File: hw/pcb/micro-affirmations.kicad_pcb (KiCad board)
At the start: 2 copper layers, 70 x 40 mm, 165 parts, among them J1 USBC, J2 DEBUG, Q1 NCH, Q10 NCH, Q2 NCH, Q3 NCH, Q4 NCH, Q5 NCH, Q6 NCH, Q7 NCH, Q8 NCH, Q9 NCH, SW1 RST, U1 STM32C031C6Tx, U2 TPS61094

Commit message: chore: exported hardware revision d files
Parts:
- moved TP7 9.78 mm to (181.4, 106.9)
- moved TP6 1.20 mm to (181.8, 100.8)
- moved G*** 0.80 mm to (159.6, 106.0)
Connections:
- TP7 pad 1: Net-(U1-PA0) -> Net-(U1-PB7)
- U1 pad 11: Net-(U1-PA0) -> CAP_VOLT
- U1 pad 46: CAP_VOLT -> Net-(U1-PB7)
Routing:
- net CAP_VOLT: track 41.0 -> 49.9 mm
- net GND: track 62.1 -> 64.6 mm
- net /CHARGE_SENSE: track 28.3 -> 25.9 mm
- net Net-(U1-PA0): track 2.30 -> 0.00 mm, vias 1 -> 0
- net +3V3: track 28.4 -> 26.3 mm, vias 1 -> 0
- net Net-(U1-PB7): track 0.00 -> 1.71 mm, vias 0 -> 1
- net Net-(U1-PC13): track 3.55 -> 2.61 mm
- net /DEBUG_SWDIO: track 23.3 -> 22.5 mm
- net /NRST: track 38.9 -> 38.1 mm
- net /MATRIX_A7: track 15.2 -> 15.9 mm

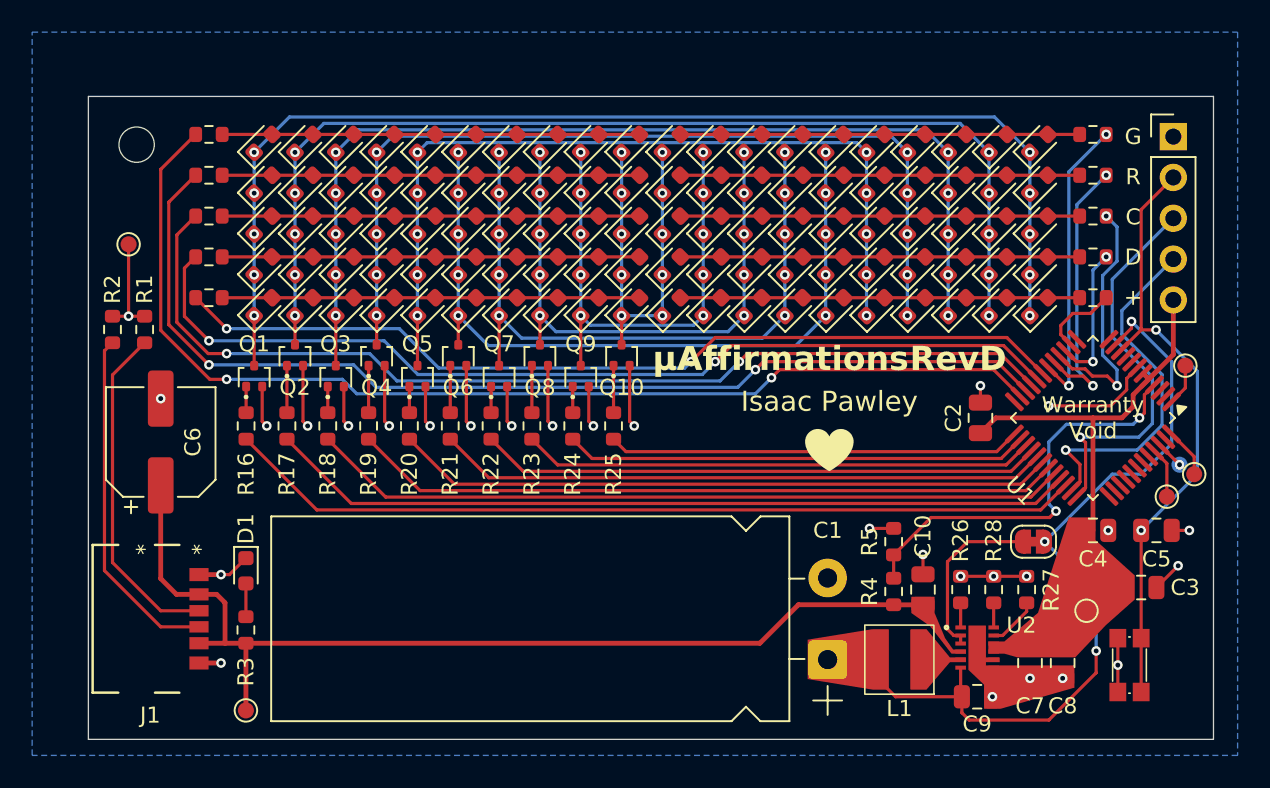
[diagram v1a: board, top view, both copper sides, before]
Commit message: fix: updated schematics to pcb revision d
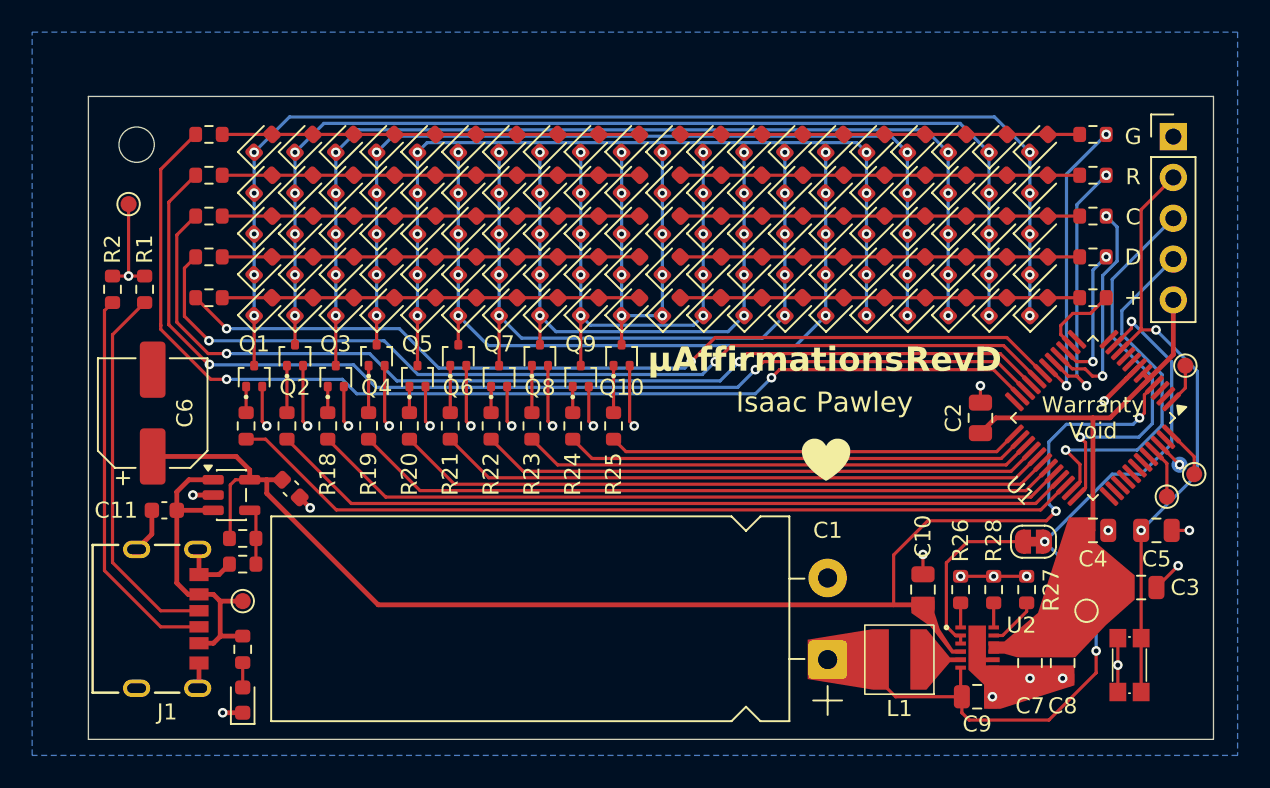
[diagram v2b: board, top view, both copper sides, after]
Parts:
- removed R4: 5.1k, Resistor_SMD:R_0603_1608Metric
- removed R5: 10k, Resistor_SMD:R_0603_1608Metric
- added C11: 1u, Capacitor_SMD:C_0603_1608Metric, F.Cu at (118.2, 109.8)
- added C12: 1u, Capacitor_SMD:C_0603_1608Metric, F.Cu at (126.1, 108.4)
- added R29: 33k, Resistor_SMD:R_0603_1608Metric, F.Cu at (123.1, 111.5)
- added R30: 10k, Resistor_SMD:R_0603_1608Metric, F.Cu at (123.1, 113.1)
- added U3: LDK130, Package_TO_SOT_SMD:SOT-23-5, F.Cu at (122.4, 108.8)
- J1: value USBC -> USB-C
- moved D1 8.05 mm to (123.1, 121.6), turned to 90 degrees
- moved TP2 6.80 mm to (123.1, 115.4)
- moved R1 2.50 mm to (117.0, 96.0)
- moved R2 2.50 mm to (115.0, 96.0)
- moved TP8 2.50 mm to (116.0, 90.7)
- moved C6 1.87 mm to (117.5, 103.7)
- moved R3 1.22 mm to (123.1, 118.4), turned to -90 degrees
- moved G*** 0.63 mm to (159.4, 106.6)
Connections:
- C10 pad 1: +5V -> /CHARGE_SENSE
- C6 pad 1: +5V -> /CHARGE_SENSE
- U2 pad 4: +5V -> /CHARGE_SENSE
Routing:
- net /CHARGE_SENSE: track 25.9 -> 85.8 mm
- net +5V: track 63.2 -> 20.2 mm
- net Net-(U3-ADJ): track 0.00 -> 3.74 mm
- net Net-(J1-CC2): track 21.7 -> 24.2 mm
- net Net-(J1-CC1): track 21.1 -> 23.6 mm
- net /MATRIX_A7: track 15.9 -> 13.8 mm
- net GND: track 64.6 -> 65.9 mm, vias 28 -> 27
- net /MATRIX_A6: track 17.3 -> 16.7 mm
- net Net-(D1-A): track 2.07 -> 1.55 mm

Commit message: fix: added or-ing diode to board
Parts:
- removed JP1: SolderJumper_2_Bridged, Jumper:SolderJumper-2_P1.3mm_Bridged_RoundedPad1.0x1.5mm
- added D2: ~, Package_TO_SOT_SMD:SOT-23, F.Cu at (165.1, 112.6)
- moved C10 3.25 mm to (162.2, 115.0)
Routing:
- net CAP_VOLT: track 49.9 -> 56.8 mm
- net /CHARGE_SENSE: track 85.8 -> 91.3 mm
- net GND: track 65.9 -> 71.1 mm, vias 27 -> 30
- net Net-(D2-K): track 10.9 -> 5.76 mm

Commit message: chore: finalised pcb for rev d export
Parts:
- removed G***: LOGO, LOGO
- R28: value 13.0k -> 13.0k*
- R29: value 33k -> 33k*
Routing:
- net /CHARGE_SENSE: track 91.3 -> 90.6 mm
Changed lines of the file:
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@@
 		(filling no)
 		(pcbplotparams
-			(layerselection 0x00000000_00000000_55555555_5755f5ff)
+			(layerselection 0x00000000_00000000_55555555_555555d0)
 			(plot_on_all_layers_selection 0x00000000_00000000_00000000_00000000)
 			(disableapertmacros no)
@@
 			(drillshape 0)
 			(scaleselection 1)
-			(outputdirectory "gerbers/RevD/")
+			(outputdirectory "gerbers/RevD-not/")
 		)
 	)
@@
 			)
 		)
-		(property "Value" "33k"
+		(property "Value" "33k*"
 			(at 0 1.43 0)
 			(layer "F.Fab")
@@
 		)
 	)
-	(footprint "LOGO"
-		(layer "F.Cu")
-		(at 159.397825 106.6)
-		(property "Reference" "G***"
-			(at 0 0 0)
-			(layer "F.SilkS")
-			(hide yes)
-			(effects
-				(font
-					(size 1.5 1.5)
-					(thickness 0.3)
-				)
-			)
-		)
-		(property "Value" "LOGO"
-			(at 0.75 0 0)
-			(layer "F.SilkS")
-			(hide yes)
-			(effects
-				(font
-					(size 1.5 1.5)
-					(thickness 0.3)
-				)
-			)
-		)
-		(property "Datasheet" ""
-			(at 0 0 0)
-			(layer "F.Fab")
-			(hide yes)
-			(effects
-				(font
-					(size 1.27 1.27)
-				)
-			)
-		)
-		(property "Description" ""
-			(at 0 0 0)
-			(layer "F.Fab")
-			(hide yes)
-			(effects
-				(font
-					(size 1.27 1.27)
-				)
-			)
-		)
-		(attr board_only exclude_from_pos_files exclude_from_bom)
-		(duplicate_pad_numbers_are_jumpers no)
-		(fp_poly
-			(pts
-				(xy 0.771563 -1.309687) (xy 0.835853 -1.302839) (xy 0.844934 -1.30143) (xy 0.909498 -1.288299) (xy 0.972175 -1.270069)
-				(xy 1.032758 -1.246845) (xy 1.091044 -1.218734) (xy 1.146829 -1.185839) (xy 1.199906 -1.148266)
-				(xy 1.250073 -1.106119) (xy 1.278387 -1.078985) (xy 1.318838 -1.035563) (xy 1.354602 -0.991192)
-				(xy 1.386458 -0.944789) (xy 1.415188 -0.895275) (xy 1.425651 -0.875014) (xy 1.451398 -0.818801)
-				(xy 1.472115 -0.7629) (xy 1.48801 -0.706469) (xy 1.499293 -0.648667) (xy 1.506173 -0.588651) (xy 1.508576 -0.541415)
-				(xy 1.507749 -0.467586) (xy 1.501492 -0.393197) (xy 1.489811 -0.318266) (xy 1.472714 -0.242808)
-				(xy 1.450209 -0.166842) (xy 1.422303 -0.090383) (xy 1.389004 -0.013449) (xy 1.350318 0.063943) (xy 1.306254 0.141776)
-				(xy 1.256819 0.220035) (xy 1.20202 0.298701) (xy 1.141865 0.377758) (xy 1.076362 0.457189) (xy 1.054578 0.482335)
-				(xy 0.98928 0.554219) (xy 0.918979 0.626625) (xy 0.844076 0.699219) (xy 0.764967 0.771666) (xy 0.682053 0.843632)
-				(xy 0.595733 0.914782) (xy 0.506404 0.984782) (xy 0.414467 1.053298) (xy 0.320321 1.119994) (xy 0.224363 1.184537)
-				(xy 0.191787 1.20568) (xy 0.173831 1.21713) (xy 0.154526 1.229268) (xy 0.134511 1.241708) (xy 0.114423 1.254065)
-				(xy 0.094901 1.265953) (xy 0.076583 1.276986) (xy 0.060106 1.286779) (xy 0.046107 1.294946) (xy 0.035227 1.301102)
-				(xy 0.028101 1.30486) (xy 0.026577 1.305552) (xy 0.008703 1.310339) (xy -0.009174 1.310364) (xy -0.016498 1.308867)
-				(xy -0.023885 1.30596) (xy -0.035356 1.300271) (xy -0.050462 1.292076) (xy -0.06875 1.281648) (xy -0.089768 1.26926)
-				(xy -0.113066 1.255186) (xy -0.138193 1.239699) (xy -0.164695 1.223072) (xy -0.192123 1.205581)
-				(xy -0.220024 1.187497) (xy -0.247948 1.169094) (xy -0.255631 1.163974) (xy -0.361281 1.091427)
-				(xy -0.46365 1.017192) (xy -0.562475 0.941493) (xy -0.657497 0.864556) (xy -0.748453 0.786609) (xy -0.835084 0.707877)
-				(xy -0.917127 0.628586) (xy -0.994322 0.548962) (xy -1.066408 0.469231) (xy -1.091317 0.440241)
-				(xy -1.156319 0.360387) (xy -1.215859 0.28074) (xy -1.269939 0.201295) (xy -1.318559 0.12205) (xy -1.361723 0.042999)
-				(xy -1.399433 -0.035861) (xy -1.43169 -0.114535) (xy -1.458497 -0.193026) (xy -1.479855 -0.27134)
-				(xy -1.495767 -0.34948) (xy -1.501471 -0.386921) (xy -1.504292 -0.412133) (xy -1.506477 -0.440744)
-				(xy -1.508004 -0.471455) (xy -1.508848 -0.50297) (xy -1.508987 -0.533992) (xy -1.508396 -0.563225)
-				(xy -1.507054 -0.589371) (xy -1.50544 -0.607041) (xy -1.498162 -0.658342) (xy -1.488425 -0.706263)
-				(xy -1.475799 -0.752259) (xy -1.459856 -0.79778) (xy -1.440167 -0.844279) (xy -1.427529 -0.870912)
-				(xy -1.401953 -0.91915) (xy -1.374172 -0.963814) (xy -1.343342 -1.006082) (xy -1.308617 -1.047134)
-				(xy -1.278366 -1.078985) (xy -1.230498 -1.123353) (xy -1.179602 -1.163279) (xy -1.125974 -1.198665)
-				(xy -1.069908 -1.229411) (xy -1.011696 -1.255422) (xy -0.951635 -1.276598) (xy -0.890016 -1.292843)
-				(xy -0.827136 -1.304057) (xy -0.763287 -1.310145) (xy -0.698764 -1.311007) (xy -0.633862 -1.306545)
-				(xy -0.605216 -1.302864) (xy -0.541709 -1.290799) (xy -0.479717 -1.27359) (xy -0.41953 -1.251421)
-				(xy -0.361439 -1.224479) (xy -0.305736 -1.192949) (xy -0.252712 -1.157018) (xy -0.202658 -1.11687)
-				(xy -0.155865 -1.072691) (xy -0.112625 -1.024667) (xy -0.073228 -0.972984) (xy -0.062003 -0.956494)
-				(xy -0.050706 -0.938917) (xy -0.039399 -0.920388) (xy -0.028708 -0.902008) (xy -0.01926 -0.884882)
-				(xy -0.01168 -0.87011) (xy -0.006763 -0.859221) (xy -0.00359 -0.852322) (xy -0.000892 -0.848192)
-				(xy -0.000068 -0.84767) (xy 0.002039 -0.849978) (xy 0.005261 -0.855918) (xy 0.007693 -0.861358)
-				(xy 0.015176 -0.877406) (xy 0.025488 -0.896692) (xy 0.038002 -0.918218) (xy 0.05209 -0.940984) (xy 0.067124 -0.963992)
-				(xy 0.082476 -0.986242) (xy 0.097519 -1.006738) (xy 0.105676 -1.017204) (xy 0.130823 -1.046493)
-				(xy 0.159878 -1.076634) (xy 0.191638 -1.106533) (xy 0.224902 -1.135095) (xy 0.258465 -1.161227)
-				(xy 0.282732 -1.178319) (xy 0.338023 -1.212108) (xy 0.39569 -1.241091) (xy 0.455374 -1.26519) (xy 0.51672 -1.284327)
-				(xy 0.579369 -1.298423) (xy 0.642964 -1.307401) (xy 0.707148 -1.311181)
-			)
-			(stroke
-				(width 0)
-				(type solid)
-			)
-			(fill yes)
-			(layer "F.SilkS")
-		)
-		(embedded_fonts no)
-	)
 	(footprint "Diode_SMD:D_0603_1608Metric"
 		(layer "F.Cu")
@@
 		(sheetname "/supercapacitor-charger/")
 		(sheetfile "supercapacitor-charger.kicad_sch")
+		(units
+			(unit
+				(name "A")
+				(pins "1" "2")
+			)
+		)
 		(attr smd)
 		(duplicate_pad_numbers_are_jumpers no)
@@
 			)
 		)
-		(property "Value" "13.0k"
+		(property "Value" "13.0k*"
 			(at 0 1.43 90)
 			(layer "F.Fab")
@@
 	)
 	(segment
-		(start 165.132182 116)
+		(start 164.15 116)
 		(end 162.2 116)
 		(width 0.3)
@@
 	)
 	(segment
-		(start 164.15 114.25)
-		(end 162.4 116)
-		(width 0.2)
-		(layer "F.Cu")
-		(net "/CHARGE_SENSE")
-	)
-	(segment
 		(start 122.69375 106.4)
 		(end 123.5375 107.24375)
@@
 	)
 	(segment
-		(start 179.2 103.7)
-		(end 179.2 102.567766)
+		(start 164.15 111.7)
+		(end 164.15 116)
 		(width 0.2)
 		(layer "F.Cu")
@@
 	)
 	(segment
-		(start 164.15 111.7)
-		(end 164.15 114.25)
+		(start 179.2 103.7)
+		(end 179.2 102.567766)
 		(width 0.2)
 		(layer "F.Cu")
@@
 	)
 	(segment
+		(start 165.132182 116)
+		(end 164.15 116)
+		(width 0.3)
+		(layer "F.Cu")
+		(net "/CHARGE_SENSE")
+	)
+	(segment
 		(start 122.325 111.45)
 		(end 122.325 108.175)
@@
 	)
 	(segment
+		(start 165.1 115.19)
+		(end 167.449622 117.539622)
+		(width 0.2)
+		(layer "F.Cu")
+		(net "Net-(D2-K)")
+	)
+	(segment
+		(start 167.767 118.039748)
+		(end 167.767 117.539622)
+		(width 0.2)
+		(layer "F.Cu")
+		(net "Net-(D2-K)")
+	)
+	(segment
+		(start 165.1 113.575001)
+		(end 165.1 115.19)
+		(width 0.2)
+		(layer "F.Cu")
+		(net "Net-(D2-K)")
+	)
+	(segment
+		(start 167.449622 117.539622)
+		(end 167.767 117.539622)
+		(width 0.2)
+		(layer "F.Cu")
+		(net "Net-(D2-K)")
+	)
+	(segment
 		(start 138.413152 107.724999)
 		(end 136.013153 105.325)
@@
 		(net "Net-(U1-PB7)")
 	)
-	(segment
-		(start 165.1 115.19)
-		(end 167.449622 117.539622)
-		(width 0.2)
-		(layer "F.Cu")
-		(net "Net-(D2-K)")
-	)
-	(segment
-		(start 167.767 118.039748)
-		(end 167.767 117.539622)
-		(width 0.2)
-		(layer "F.Cu")
-		(net "Net-(D2-K)")
-	)
-	(segment
-		(start 165.1 113.575001)
-		(end 165.1 115.19)
-		(width 0.2)
-		(layer "F.Cu")
-		(net "Net-(D2-K)")
-	)
-	(segment
-		(start 167.449622 117.539622)
-		(end 167.767 117.539622)
-		(width 0.2)
-		(layer "F.Cu")
-		(net "Net-(D2-K)")
-	)
 	(zone
